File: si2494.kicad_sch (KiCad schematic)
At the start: 16 parts, among them J2 Conn_02x02_Odd_Even, SW2 SW_Push, U1 Si2494-A-FM, U4 25LC640AT-E/SN, U7 DS1818, X1 ECS-2520MV-xxx-xx

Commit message: Sent to fab v3.0
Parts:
- C11, C50, C52: DIGIKEY 2679-C0603X7R160-104MNETR-ND -> 2679-C0603X7R160-104MNE-CT-ND
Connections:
- net AOUT: no longer names the net of U1.15 (AOUT)
- net nINT: no longer names the net of U1.35 (nINT)
- no-connect marks 13 -> 15
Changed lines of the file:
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@@
   (no_connect (at 170.18 46.99))
   (no_connect (at 220.98 96.52))
+  (no_connect (at 170.18 110.49))
   (no_connect (at 250.19 102.87))
   (no_connect (at 170.18 72.39))
+  (no_connect (at 170.18 64.77))
   (no_connect (at 170.18 69.85))
   (no_connect (at 170.18 34.29))
@@
     (effects (font (size 1.27 1.27)) (justify right bottom))
   )
-  (label "nINT" (at 170.18 64.77 180) (fields_autoplaced)
-    (effects (font (size 1.27 1.27)) (justify right bottom))
-  )
   (label "nRI" (at 170.18 105.41 180) (fields_autoplaced)
-    (effects (font (size 1.27 1.27)) (justify right bottom))
-  )
-  (label "AOUT" (at 170.18 110.49 180) (fields_autoplaced)
     (effects (font (size 1.27 1.27)) (justify right bottom))
   )
@@
       (effects (font (size 1.27 1.27)) hide)
     )
-    (property "DIGIKEY" "2679-C0603X7R160-104MNETR-ND" (at 214.63 24.13 0)
+    (property "DIGIKEY" "2679-C0603X7R160-104MNE-CT-ND" (at 214.63 24.13 0)
       (effects (font (size 1.27 1.27)) hide)
     )
@@
       (effects (font (size 1.27 1.27)) hide)
     )
-    (property "DIGIKEY" "2679-C0603X7R160-104MNETR-ND" (at 203.2 24.13 0)
+    (property "DIGIKEY" "2679-C0603X7R160-104MNE-CT-ND" (at 203.2 24.13 0)
       (effects (font (size 1.27 1.27)) hide)
     )
@@
       (effects (font (size 1.27 1.27)) hide)
     )
-    (property "DIGIKEY" "2679-C0603X7R160-104MNETR-ND" (at 254 102.87 0)
-      (effects (font (size 1.27 1.27)) hide)
-    )
+    (property "DIGIKEY" "2679-C0603X7R160-104MNE-CT-ND" (at 254 102.87 0)
+      (effects (font (size 1.27 1.27)) hide)
+    )

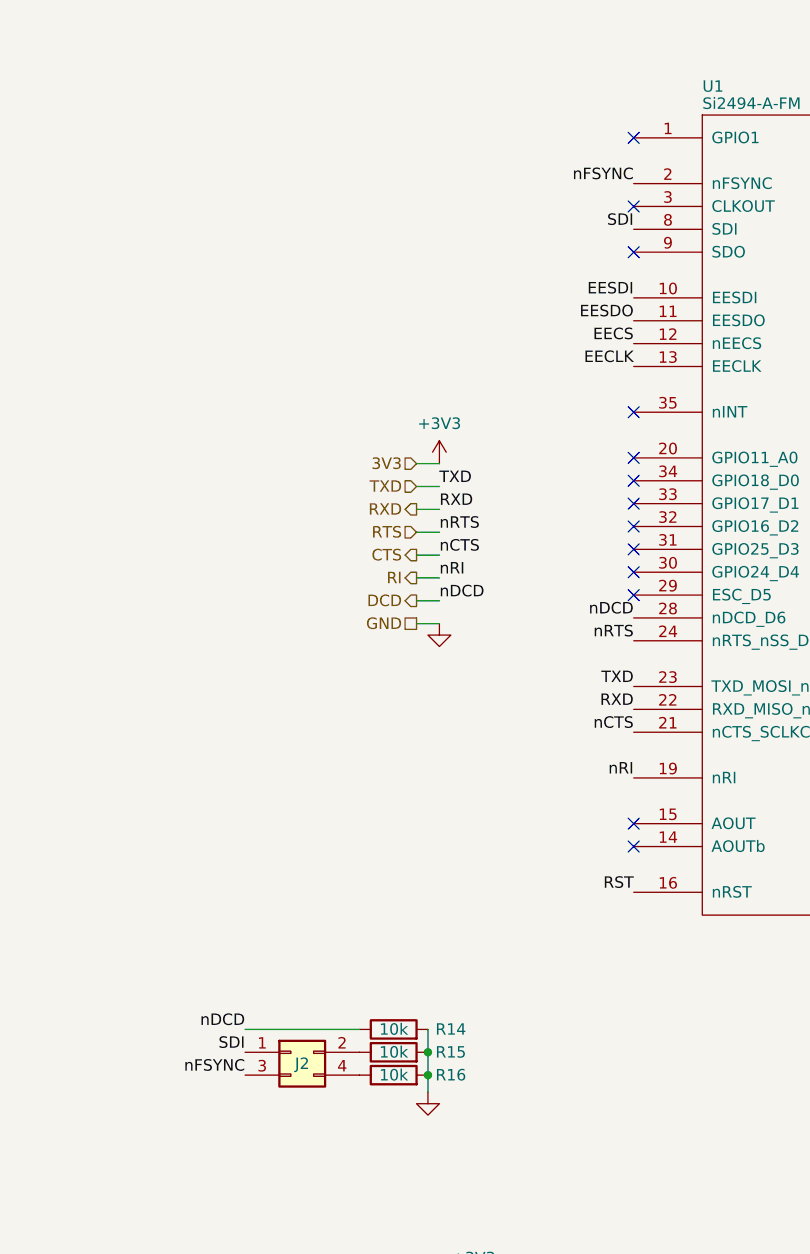
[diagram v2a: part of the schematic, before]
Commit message: [4.0] M.2 Module. Sent to fab
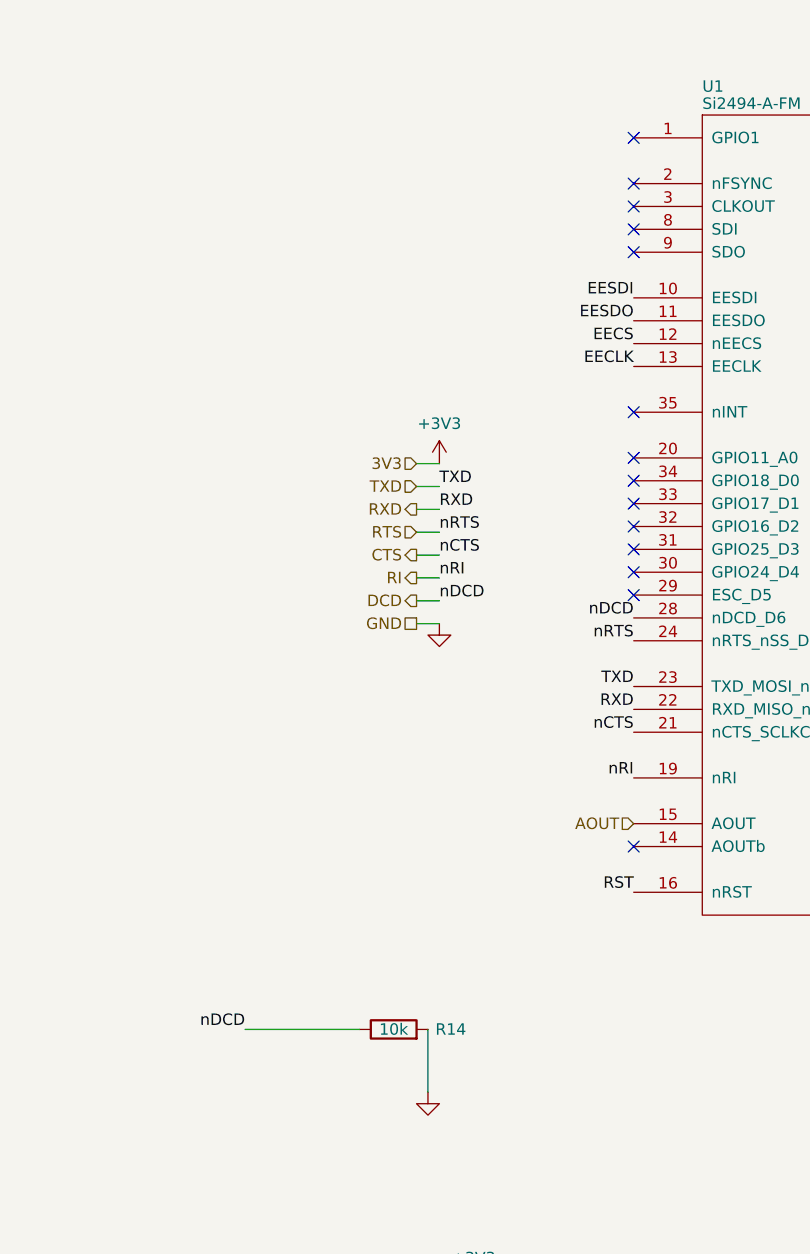
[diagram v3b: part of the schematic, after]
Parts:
- removed J2: Conn_02x02_Odd_Even, Connector_PinHeader_2.54mm:PinHeader_2x02_P2.54mm_Vertical, symbol Connector_Generic:Conn_02x02_Odd_Even
- removed R15, R16: 10k, Resistor_SMD:R_0603_1608Metric, symbol Device:R
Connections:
- net AOUT: now reaches U1.15 (AOUT)
- net SDI: no longer names the net of U1.8 (SDI)
- net nFSYNC: no longer names the net of U1.2 (nFSYNC)
- no-connect marks 15 -> 16
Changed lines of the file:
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@@
 (kicad_sch (version 20230121) (generator eeschema)
-  (paper "A4")
+  (paper "USLetter")
   (title_block
     (title "SkyFax")
-    (date "2023-09-02")
-    (rev "3.0")
+    (date "2023-09-12")
+    (rev "4.0")
     (company "Brian Hong")
     (comment 1 "@im_eningeer")
   )
-  (junction (at 147.32 135.89) (diameter 0) (color 0 0 0 0)
-  )
   (junction (at 240.03 95.25) (diameter 0) (color 0 0 0 0)
   )
@@
   (junction (at 222.25 127) (diameter 0) (color 0 0 0 0)
   )
-  (junction (at 147.32 138.43) (diameter 0) (color 0 0 0 0)
-  )
   (junction (at 195.58 21.59) (diameter 0) (color 0 0 0 0)
   )
@@
   )
   (no_connect (at 170.18 80.01))
+  (no_connect (at 170.18 39.37))
   (no_connect (at 170.18 46.99))
   (no_connect (at 220.98 96.52))
-  (no_connect (at 170.18 110.49))
   (no_connect (at 250.19 102.87))
   (no_connect (at 170.18 72.39))
+  (no_connect (at 170.18 44.45))
   (no_connect (at 170.18 64.77))
   (no_connect (at 170.18 69.85))
@@
     (stroke (width 0) (type default))
   )
-  (wire (pts (xy 147.32 138.43) (xy 147.32 140.335))
-    (stroke (width 0) (type default))
-  )
   (wire (pts (xy 238.76 127) (xy 238.76 128.27))
     (stroke (width 0) (type default))
@@
     (stroke (width 0) (type default))
   )
-  (wire (pts (xy 147.32 133.35) (xy 147.32 135.89))
-    (stroke (width 0) (type default))
-  )
   (wire (pts (xy 142.24 170.815) (xy 137.16 170.815))
     (stroke (width 0) (type default))
@@
     (stroke (width 0) (type default))
   )
-  (wire (pts (xy 147.32 135.89) (xy 147.32 138.43))
+  (wire (pts (xy 147.32 133.35) (xy 147.32 140.335))
     (stroke (width 0) (type default))
   )
@@
     (effects (font (size 1.27 1.27)) (justify right bottom))
   )
-  (label "SDI" (at 127 135.89 180) (fields_autoplaced)
-    (effects (font (size 1.27 1.27)) (justify right bottom))
-  )
   (label "EECLK" (at 170.18 59.69 180) (fields_autoplaced)
     (effects (font (size 1.27 1.27)) (justify right bottom))
@@
     (effects (font (size 1.27 1.27)) (justify left bottom))
   )
-  (label "nFSYNC" (at 127 138.43 180) (fields_autoplaced)
-    (effects (font (size 1.27 1.27)) (justify right bottom))
-  )
   (label "EESDO" (at 170.18 54.61 180) (fields_autoplaced)
     (effects (font (size 1.27 1.27)) (justify right bottom))
@@
     (effects (font (size 1.27 1.27)) (justify left bottom))
   )
-  (label "nFSYNC" (at 170.18 39.37 180) (fields_autoplaced)
-    (effects (font (size 1.27 1.27)) (justify right bottom))
-  )
   (label "TXD" (at 170.18 95.25 180) (fields_autoplaced)
     (effects (font (size 1.27 1.27)) (justify right bottom))
@@
     (effects (font (size 1.27 1.27)) (justify right bottom))
   )
-  (label "SDI" (at 170.18 44.45 180) (fields_autoplaced)
-    (effects (font (size 1.27 1.27)) (justify right bottom))
-  )
   (hierarchical_label "C1A" (shape bidirectional) (at 220.98 58.42 0) (fields_autoplaced)
     (effects (font (size 1.27 1.27)) (justify left))
@@
   )
   (hierarchical_label "RTS" (shape input) (at 146.05 78.105 180) (fields_autoplaced)
+    (effects (font (size 1.27 1.27)) (justify right))
+  )
+  (hierarchical_label "AOUT" (shape input) (at 170.18 110.49 180) (fields_autoplaced)
     (effects (font (size 1.27 1.27)) (justify right))
   )
@@
     )
   )
-  (symbol (lib_id "Device:R") (at 143.51 135.89 90) (unit 1)
-    (in_bom yes) (on_board yes) (dnp no)
-    (property "Reference" "R15" (at 149.86 135.89 90)
-      (effects (font (size 1.27 1.27)))
-    )
-    (property "Value" "10k" (at 143.51 135.89 90)
-      (effects (font (size 1.27 1.27)))
-    )
-    (property "Footprint" "Resistor_SMD:R_0603_1608Metric" (at 143.51 137.668 90)
-      (effects (font (size 1.27 1.27)) hide)
-    )
-    (property "Datasheet" "~" (at 143.51 135.89 0)
-      (effects (font (size 1.27 1.27)) hide)
-    )
-    (property "DIGIKEY" "RNCP0603FTD10K0CT-ND" (at 143.51 135.89 0)
-      (effects (font (size 1.27 1.27)) hide)
-    )
-    (pin "1")
-    (pin "2")
-    (instances
-      (project "SkyFax"
-        (path "/8648f108-1e45-4954-a197-b251f5522881"
-          (reference "R15") (unit 1)
-        )
-        (path "/8648f108-1e45-4954-a197-b251f5522881/a903dc45-63a8-4bd9-abb6-8c8172debdba"
-          (reference "R15") (unit 1)
-        )
-        (path "/8648f108-1e45-4954-a197-b251f5522881/dce568ae-6901-43dd-b126-62f53dd263d4"
-          (reference "R203") (unit 1)
-        )
-      )
-    )
-  )
   (symbol (lib_id "power:+3V3") (at 148.59 70.485 0) (unit 1)
     (in_bom yes) (on_board yes) (dnp no)
@@
         )
       )
-    )
-  )
-  (symbol (lib_id "Connector_Generic:Conn_02x02_Odd_Even") (at 132.08 135.89 0) (unit 1)
-    (in_bom yes) (on_board yes) (dnp no)
-    (property "Reference" "J2" (at 133.35 137.16 0)
-      (effects (font (size 1.27 1.27)))
-    )
-    (property "Value" "Conn_02x02_Odd_Even" (at 133.35 132.08 0)
-      (effects (font (size 1.27 1.27)) hide)
-    )
-    (property "Footprint" "Connector_PinHeader_2.54mm:PinHeader_2x02_P2.54mm_Vertical" (at 132.08 135.89 0)
-      (effects (font (size 1.27 1.27)) hide)
-    )
-    (property "Datasheet" "~" (at 132.08 135.89 0)
-      (effects (font (size 1.27 1.27)) hide)
-    )
-    (pin "1")
-    (pin "2")
-    (pin "3")
-    (pin "4")
-    (instances
-      (project "SkyFax"
-        (path "/8648f108-1e45-4954-a197-b251f5522881"
-          (reference "J2") (unit 1)
-        )
-        (path "/8648f108-1e45-4954-a197-b251f5522881/a903dc45-63a8-4bd9-abb6-8c8172debdba"
-          (reference "J4") (unit 1)
-        )
-        (path "/8648f108-1e45-4954-a197-b251f5522881/dce568ae-6901-43dd-b126-62f53dd263d4"
-          (reference "J2") (unit 1)
-        )
-      )
-    )
-  )
-  (symbol (lib_id "Device:R") (at 143.51 138.43 90) (unit 1)
-    (in_bom yes) (on_board yes) (dnp no)
-    (property "Reference" "R16" (at 149.86 138.43 90)
-      (effects (font (size 1.27 1.27)))
-    )
-    (property "Value" "10k" (at 143.51 138.43 90)
-      (effects (font (size 1.27 1.27)))
-    )
-    (property "Footprint" "Resistor_SMD:R_0603_1608Metric" (at 143.51 140.208 90)
-      (effects (font (size 1.27 1.27)) hide)
-    )
-    (property "Datasheet" "~" (at 143.51 138.43 0)
-      (effects (font (size 1.27 1.27)) hide)
-    )
-    (property "DIGIKEY" "RNCP0603FTD10K0CT-ND" (at 143.51 138.43 0)
-      (effects (font (size 1.27 1.27)) hide)
-    )
-    (pin "1")
-    (pin "2")
-    (instances
-      (project "SkyFax"
-        (path "/8648f108-1e45-4954-a197-b251f5522881"
-          (reference "R16") (unit 1)
-        )
-        (path "/8648f108-1e45-4954-a197-b251f5522881/a903dc45-63a8-4bd9-abb6-8c8172debdba"
-          (reference "R16") (unit 1)
-        )
-        (path "/8648f108-1e45-4954-a197-b251f5522881/dce568ae-6901-43dd-b126-62f53dd263d4"
-          (reference "R204") (unit 1)
-        )
-      )
